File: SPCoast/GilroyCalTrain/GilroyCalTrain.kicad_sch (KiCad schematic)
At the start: 38 parts, among them SW771 771, SW773 773, SW775 775

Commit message: fix(kicad): GilroyCalTrain yard circuits TK1..TK3 become 01T..03T
Each TK circuit shares a net with the Rule 93 yard marker the owner named
Track 1..3, so the zero-prefixed form 0<n>T follows the crew's track numbers.
Desk IndicationToken follows.

Verified: netlist pairs TK1/Track 1, TK2/Track 2, TK3/Track 3; desk col 2
lamps now carry 01T, 02T, 03T.

Co-Authored-By: Claude Sonnet 5.5 <noreply@anthropic.com>
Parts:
- TC2: value TK1 -> 01T
- TC3: value TK2 -> 02T
- TC4: value TK3 -> 03T
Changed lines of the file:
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@@
 			)
 		)
-		(property "Value" "TK1"
+		(property "Value" "01T"
 			(at 198.63 105.16 0)
 			(show_name no)
@@
 			)
 		)
-		(property "Value" "TK2"
+		(property "Value" "02T"
 			(at 198.63 88.65 0)
 			(show_name no)
@@
 			)
 		)
-		(property "Value" "TK3"
+		(property "Value" "03T"
 			(at 198.63 72.14 0)
 			(show_name no)

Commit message: SPCoast: owner's edits: schematics synced with the revised symbol libraries (baseline)
Update Symbols from Library on all plant and desk sheets; CP values for
Christopher, GilroyInterchange and Luchessa; Restricted Speed markers
consolidated in Corporal, Luchessa and Sargent.

Observed in the diff, not changed by the sweep that follows: CP changed on 23
symbols (Christopher: prefix removed, 815/815A/IND now Christopher North) and
added on 12 (GilroyInterchange); two lamps' Color reset to their symbol variant
(Christopher LMP93 red -> yellow, Sargent LMP133 yellow -> red).

Verified: netlists keep their net counts (Christopher 33, Corporal 26,
GilroyCalTrain 27, GilroyInterchange 22, Luchessa 34, Sargent 18, Watsonville
96, South-cTc 341); desk compiles to 75 appliances, 137 bindings, 14 columns;
no root-UUID regression.

Co-Authored-By: Claude Sonnet 5.5 <noreply@anthropic.com>
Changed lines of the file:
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@@
 			)
 		)
-		(property "Description" "Insulated Rail Joint"
+		(property "Description" "Insulated Rail Joint with Signal"
 			(at 69.85 59.69 0)
 			(hide yes)
@@
 		)
 		(property "CP" "Gilroy Caltrain"
-			(at 71.755 61.595 0)
+			(at 69.85 57.15 0)
 			(show_name no)
 			(do_not_autoplace no)
@@
 					(color 72 72 72 1)
 				)
-				(justify right)
 			)
 		)
@@
 			)
 		)
-		(property "Description" "Insulated Rail Joint"
+		(property "Description" "Insulated Rail Joint with Signal"
 			(at 190.5 107.95 0)
 			(hide yes)
@@
 		)
 		(property "CP" "Gilroy Caltrain"
-			(at 188.595 106.045 0)
+			(at 190.5 110.49 0)
 			(show_name no)
 			(do_not_autoplace no)
@@
 					(color 72 72 72 1)
 				)
-				(justify right)
 			)
 		)
@@
 		(property "Kind" "RULE_93"
 			(at 191.77 104.14 0)
+			(hide yes)
 			(show_name no)
 			(do_not_autoplace yes)
@@
 		(property "Kind" "RULE_93"
 			(at 193.04 87.63 0)
+			(hide yes)
 			(show_name no)
 			(do_not_autoplace yes)
@@
 			)
 		)
-		(property "Description" "Insulated Rail Joint"
+		(property "Description" "Insulated Rail Joint with Signal"
 			(at 191.77 91.44 0)
 			(hide yes)
@@
 		)
 		(property "CP" "Gilroy Caltrain"
-			(at 189.865 89.535 0)
+			(at 191.77 93.98 0)
 			(show_name no)
 			(do_not_autoplace no)
@@
 					(color 72 72 72 1)
 				)
-				(justify right)
 			)
 		)
@@
 			)
 		)
-		(property "Description" "Insulated Rail Joint"
+		(property "Description" "Insulated Rail Joint with Signal"
 			(at 191.77 74.93 0)
 			(hide yes)
@@
 		)
 		(property "CP" "Gilroy Caltrain"
-			(at 189.865 73.025 0)
+			(at 191.77 77.47 0)
 			(show_name no)
 			(do_not_autoplace no)
@@
 					(color 72 72 72 1)
 				)
-				(justify right)
 			)
 		)
@@
 			)
 		)
-		(property "Description" "Insulated Rail Joint"
+		(property "Description" "Insulated Rail Joint with Signal"
 			(at 185.42 59.69 0)
 			(hide yes)
@@
 		)
 		(property "CP" "Gilroy Caltrain"
-			(at 183.515 57.785 0)
+			(at 185.42 62.23 0)
 			(show_name no)
 			(do_not_autoplace no)
@@
 					(color 72 72 72 1)
 				)
-				(justify right)
 			)
 		)
@@
 		(property "Kind" "RULE_93"
 			(at 193.04 71.12 0)
+			(hide yes)
 			(show_name no)
 			(do_not_autoplace yes)
@@
 			)
 		)
-		(property "Description" "Maintainer Bungalow"
-			(at 69.85 40.01 0)
-			(hide yes)
-			(show_name no)
+		(property "Description" "Rrepresents the Control Point Maintainer Bungalow (plus optional Maintainer Call)"
+			(at 69.85 40.005 0)
+			(hide yes)
+			(show_name no)

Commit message: chore(kicad): sweep instance Role/Kind and stale fields to the library vocabulary
Scripted, one pass over every sheet except Watsonville (open in KiCad, locked):
- Role/Kind of placed symbols refreshed from the library by lib_id: 10 Role
  (MAIN HOUSE CONTROLLED_POINT -> CONTROL_POINT, Rule251-DoT empty) and 17 Kind
  (IRJ-Signal IRJ -> IRJ_SIGNAL x7, Mast_Single/Double swaps, HandThrow
  -> SWITCH_MANUAL, Derail, PanelLock -> LOCK_LEVER, NextCP).
- Stale instance fields dropped where the library no longer has them: 39 Name,
  28 Direction (all empty or retired), 5 CP on Bumper and IRJ symbols.
- Orphan embedded copies of the retired symbol Rule6.28-OtherThanMain removed
  from two sheets (unused).

Not done: Watsonville (locked); CMRInet -> CMRI (library Kind still CMRInet);
fields new to the library (MAIN HOUSE Kind, switch Indications) are not copied
onto instances, the compiler will read library defaults by lib_id; Rulebook
fields stay until the compiler stops requiring them.

Verified: per-symbol before/after comparison shows only these changes, same
symbol sets, positions and lib_ids; netlists keep their net counts (Christopher
33, Corporal 26, GilroyCalTrain 27, GilroyInterchange 22, Luchessa 34, Sargent
18, South-cTc 341); desk still 75 appliances, 137 bindings, 14 columns.

Co-Authored-By: Claude Sonnet 5.5 <noreply@anthropic.com>
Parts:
- B1, B2, B3, B4, B8: Kind IRJ -> IRJ_SIGNAL
- B5, B6, B7: CP Gilroy Caltrain -> (none)
- DOT4, DOT5, DOT6: Name Yard Limits -> (none)
- HOUSE1: Role CONTROLLED_POINT -> CONTROL_POINT
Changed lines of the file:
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@@
 			)
 		)
-		(property "CP" "Gilroy Caltrain"
-			(at 213.36 107.95 0)
-			(hide yes)
-			(show_name no)
-			(do_not_autoplace no)
-			(effects
-				(font
-					(size 1.27 1.27)
-				)
-			)
-		)
 		(pin "2"
 		)
@@
 			)
 		)
-		(property "Kind" "IRJ"
+		(property "Kind" "IRJ_SIGNAL"
 			(at 69.85 59.69 0)
 			(hide yes)
@@
 			)
 		)
-		(property "Kind" "IRJ"
+		(property "Kind" "IRJ_SIGNAL"
 			(at 190.5 107.95 0)
 			(hide yes)
@@
 			)
 		)
-		(property "Name" "Yard Limits"
-			(at 193.04 100.965 0)
-			(hide yes)
-			(show_name no)
-			(do_not_autoplace no)
-			(effects
-				(font
-					(size 1.27 1.27)
-				)
-			)
-		)
 		(property "Role" "POLICY"
 			(at 191.77 110.49 0)
@@
 			)
 		)
-		(property "Name" "Yard Limits"
-			(at 194.31 84.455 0)
-			(hide yes)
-			(show_name no)
-			(do_not_autoplace no)
-			(effects
-				(font
-					(size 1.27 1.27)
-				)
-			)
-		)
 		(property "Role" "POLICY"
 			(at 193.04 93.98 0)
@@
 			)
 		)
-		(property "Kind" "IRJ"
+		(property "Kind" "IRJ_SIGNAL"
 			(at 191.77 91.44 0)
 			(hide yes)
@@
 			)
 		)
-		(property "Kind" "IRJ"
+		(property "Kind" "IRJ_SIGNAL"
 			(at 191.77 74.93 0)
 			(hide yes)
@@
 			)
 		)
-		(property "Kind" "IRJ"
+		(property "Kind" "IRJ_SIGNAL"
 			(at 185.42 59.69 0)
 			(hide yes)
@@
 			)
 		)
-		(property "Name" "Yard Limits"
-			(at 194.31 67.945 0)
-			(hide yes)
-			(show_name no)
-			(do_not_autoplace no)
-			(effects
-				(font
-					(size 1.27 1.27)
-				)
-			)
-		)
 		(property "Role" "POLICY"
 			(at 193.04 77.47 0)
@@
 			)
 		)
-		(property "CP" "Gilroy Caltrain"
-			(at 213.36 91.44 0)
-			(hide yes)
-			(show_name no)
-			(do_not_autoplace no)
-			(effects
-				(font
-					(size 1.27 1.27)
-				)
-			)
-		)
 		(pin "2"
 		)
@@
 			)
 		)
-		(property "Role" "CONTROLLED_POINT"
+		(property "Role" "CONTROL_POINT"
 			(at 69.85 34.29 0)
 			(hide yes)
@@
 			(at 213.36 74.93 0)
 			(hide yes)
-			(show_name no)
-			(do_not_autoplace no)
-			(effects
-				(font
-					(size 1.27 1.27)
-				)
-			)
-		)
-		(property "CP" "Gilroy Caltrain"
-			(at 213.36 74.93 0)
-			(hide yes)

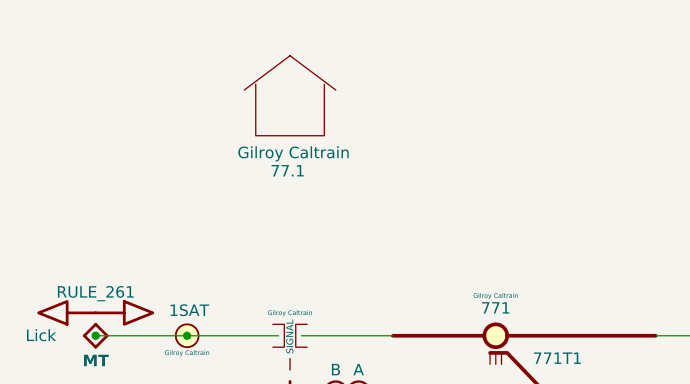
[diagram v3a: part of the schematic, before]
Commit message: SPCoast: owner's edits: Interlocking symbol on every Trackplan; MAIN HOUSE is STRUCTURE/CONTROL_POINT (baseline)
Each plant has one Interlocking symbol (Value is the authoritative name) and
every MAIN HOUSE's Interlocking pin is wired to it. Library Role/Kind:
Interlocking is STRUCTURE/INTERLOCKING, MAIN HOUSE is STRUCTURE/CONTROL_POINT
(refreshed on all instances by the owner).

Verified: one Interlocking symbol per plant; every house shares a net with it;
net counts are one higher than before in each plant (Christopher 34, Corporal
27, GilroyCalTrain 28, GilroyInterchange 23, Luchessa 35, Sargent 19,
Watsonville 97); no root-UUID regression; no symbol moved or removed.

Co-Authored-By: Claude Sonnet 5.5 <noreply@anthropic.com>
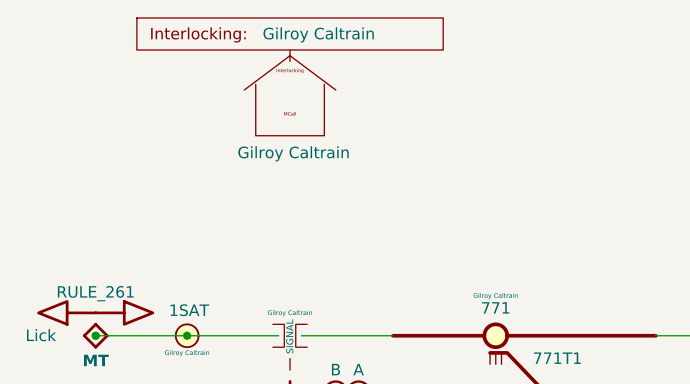
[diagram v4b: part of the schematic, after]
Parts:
- added Plant1: ${TITLE}, symbol Railroad:Interlocking
- HOUSE1: Kind (none) -> CONTROL_POINT; Role CONTROL_POINT -> STRUCTURE
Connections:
- new net: HOUSE1.2 (Interlocking), Plant1.1 (Interlocking)
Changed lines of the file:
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@@
+	)
+	(symbol
+		(lib_id "Railroad:Interlocking")
+		(at 69.85 29.21 0)
+		(unit 1)
+		(body_style 1)
+		(exclude_from_sim no)
+		(in_bom yes)
+		(on_board yes)
+		(in_pos_files yes)
+		(dnp no)
+		(fields_autoplaced yes)
+		(property "Reference" "Plant1"
+			(at 55.626 23.368 0)
+			(hide yes)
+			(show_name no)
+			(do_not_autoplace no)
+			(effects
+				(font
+					(size 1.27 1.27)
+				)
+			)
+		)
+		(property "Value" "${TITLE}"
+			(at 66.802 26.162 0)
+			(show_name no)
+			(do_not_autoplace yes)
+			(effects
+				(font
+					(size 1.27 1.27)
+				)
+				(justify left)
+			)
+		)
+		(property "Footprint" ""
+			(at 69.85 29.21 0)
+			(hide yes)
+			(show_name no)
+			(do_not_autoplace no)
+			(effects
+				(font
+					(size 1.27 1.27)
+				)
+			)
+		)
+		(property "Datasheet" ""
+			(at 69.85 29.21 0)
+			(hide yes)
+			(show_name no)
+			(do_not_autoplace no)
+			(effects
+				(font
+					(size 1.27 1.27)
+				)
+			)
+		)
+		(property "Description" ""
+			(at 69.85 29.21 0)
+			(hide yes)
+			(show_name no)
+			(do_not_autoplace no)
+			(effects
+				(font
+					(size 1.27 1.27)
+				)
+			)
+		)
+		(property "Role" "STRUCTURE"
+			(at 58.547 19.558 0)
+			(hide yes)
+			(show_name no)
+			(do_not_autoplace no)
+			(effects
+				(font
+					(size 1.27 1.27)
+				)
+			)
+		)
+		(property "Kind" "INTERLOCKING"
+			(at 59.944 21.209 0)
+			(hide yes)
+			(show_name no)
+			(do_not_autoplace no)
+			(effects
+				(font
+					(size 1.27 1.27)
+				)
+			)
+		)
+		(pin "1"
+		)
+		(instances
+			(project "GilroyCalTrain"
+				(path "/2483c39b-4890-45a3-8f90-421e08f2026a"
+					(reference "Plant1")
+					(unit 1)
+				)
+			)
+		)
 	)
 	(symbol
@@
 			)
 		)
-		(property "Description" "Rrepresents the Control Point Maintainer Bungalow (plus optional Maintainer Call)"
+		(property "Description" "The Control Point Maintainer Bungalow (plus optional Maintainer Call)"
 			(at 69.85 40.005 0)
 			(hide yes)
@@
 		)
 		(property "Milepost" "77.1"
-			(at 69.596 41.402 0)
-			(show_name no)
-			(do_not_autoplace no)
-			(effects
-				(font
-					(size 1.27 1.27)
-				)
-			)
-		)
-		(property "Role" "CONTROL_POINT"
-			(at 69.85 34.29 0)
+			(at 69.85 40.005 0)
+			(hide yes)
+			(show_name no)
+			(do_not_autoplace no)
+			(effects
+				(font
+					(size 1.27 1.27)
+				)
+			)
+		)
+		(property "Role" "STRUCTURE"
+			(at 54.61 31.75 0)
+			(hide yes)
+			(show_name no)
+			(do_not_autoplace no)
+			(effects
+				(font
+					(size 1.27 1.27)
+				)
+			)
+		)
+		(property "Kind" "CONTROL_POINT"
+			(at 56.515 33.782 0)
 			(hide yes)
 			(show_name no)
@@
 		(pin "1"
 		)
+		(pin "2"
+		)
 		(instances

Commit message: SPCoast: owner's edits: NextCP names, Christopher heads and masts, Sargent milepost, Watsonville circuits and desk tokens (baseline)
- NextCP values name interlockings: GilroyCalTrain CP2 -> Gilroy Interchange;
  Luchessa CP1 -> Gilroy Interchange, CP2 -> Hollister, CP3 and CP4 ->
  Christopher.
- Christopher: the two unnamed dwarf masts, their IRJ-Signals (now plain IRJs)
  and heads removed; remaining heads lettered A, B, C.
- Sargent MAIN HOUSE Milepost 83.5.
- Watsonville circuits SDT -> 0DT and SAT -> 0AT; desk tokens 0DT, 0AT, AT and
  Watsonville:837T1 follow.

Verified: netlists rebuild (Christopher 30, Corporal 27, GilroyCalTrain 28,
GilroyInterchange 23, Luchessa 35, Sargent 19, Watsonville 97, South-cTc 341);
Christopher has no mast or head diagnostics left; desk compiles to 75
appliances, 137 bindings, 14 columns; no root-UUID regression.

Co-Authored-By: Claude Sonnet 5.5 <noreply@anthropic.com>
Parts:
- CP2: value Gilroy North -> Gilroy Interchange
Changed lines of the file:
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@@
 			)
 		)
-		(property "Value" "Gilroy North"
+		(property "Value" "Gilroy Interchange"
 			(at 208.28 59.6899 0)
 			(show_name no)

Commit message: chore(kicad): refresh instances to the ADR 0003 libraries (InterlockingPlant 95f53e2)
- Desk sheets (South-cTc/*) and the Sargent sandbox: embedded PanelSwitch, PanelLock,
  PanelSignal, PanelMCall, PanelCode, PanelLamp-*, PanelColumn-MAX7313 definitions refreshed
  from the library (refresh_embedded.py, checked against the pre-pass library: only Description
  text had drifted). Instance Role APPLIANCE -> PANEL (77).
- Plant sheets: powered-switch instance Kind SWITCH_POWERED -> SWITCH_REMOTE (21), matching the
  library (sweep_role_kind_fields.py).

Verified:
- verify_symbol_diff.py: same symbols, lib_ids and positions; only Role/Kind changed.
- Nets unchanged: Christopher 30, Corporal 27, GilroyCalTrain 28, GilroyInterchange 23,
  Luchessa 35, Sargent 61, Watsonville 99, South-cTc 341.
- parse_kicad_plant.py --format text identical before/after for all seven plants.
- Desk compile 75/137/14, diagnostics identical; the 7 desk locks bind WLS/~{WLS}/~{WLK}/WLK
  to the bits that were NWS/RWS/RWK/NWK.
- No sheet or project outside Luchessa carries the copied root UUID.

Co-Authored-By: Claude Opus 5.5 <noreply@anthropic.com>
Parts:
- SW771, SW773, SW775: Kind SWITCH_POWERED -> SWITCH_REMOTE
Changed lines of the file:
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@@
 			)
 		)
-		(property "Kind" "SWITCH_POWERED"
+		(property "Kind" "SWITCH_REMOTE"
 			(at 140.97 91.44 0)
 			(hide yes)
@@
 			)
 		)
-		(property "Kind" "SWITCH_POWERED"
+		(property "Kind" "SWITCH_REMOTE"
 			(at 172.72 91.44 0)
 			(hide yes)
@@
 			)
 		)
-		(property "Kind" "SWITCH_POWERED"
+		(property "Kind" "SWITCH_REMOTE"
 			(at 92.71 59.69 0)
 			(hide yes)
